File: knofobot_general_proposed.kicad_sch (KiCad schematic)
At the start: 8 parts, among them M1 Motor_DC, M2 Motor_DC, U1 L298N, U2 HC-SR04, U3 HC-SR04, U4 VL53L0CXV0DH1

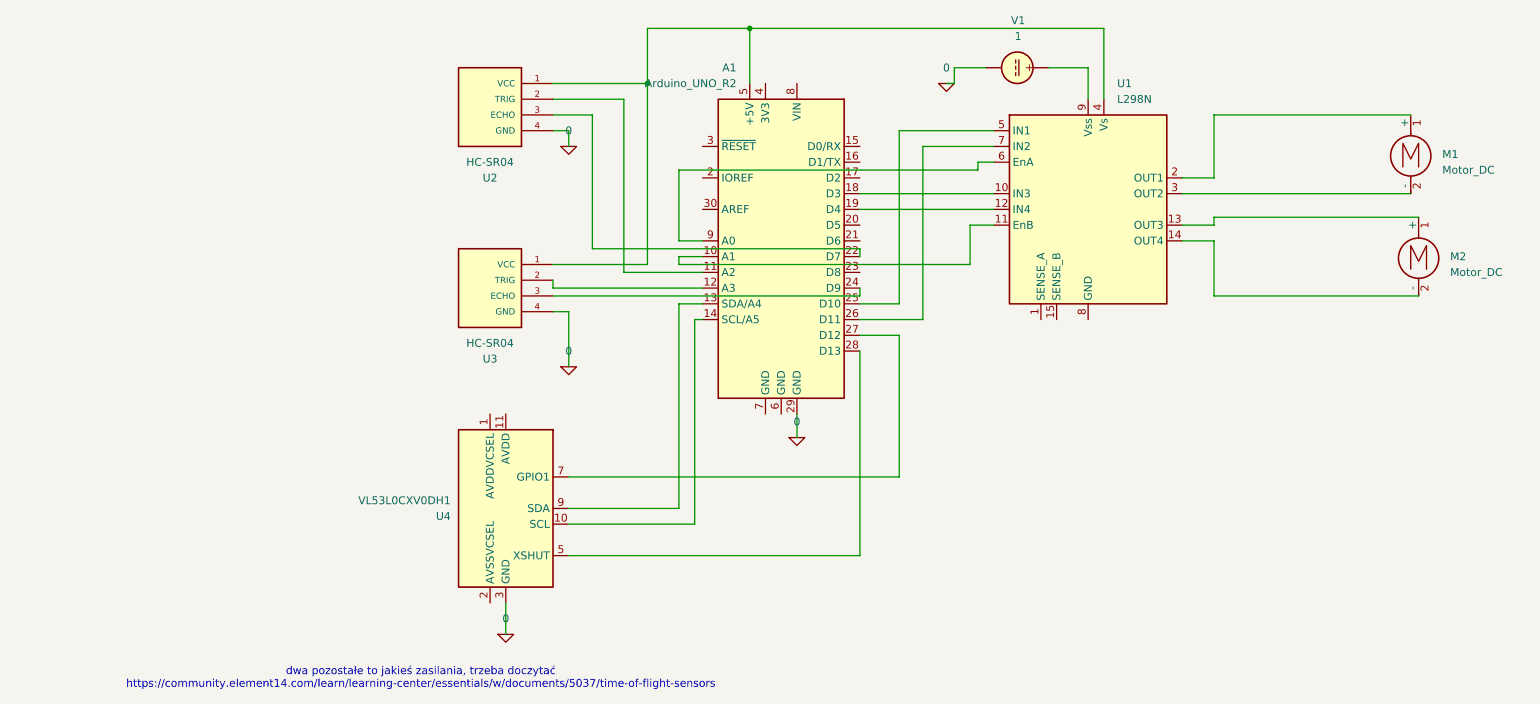
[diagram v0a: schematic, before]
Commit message: proposed new wiring minimising changes w/ 2 sensors
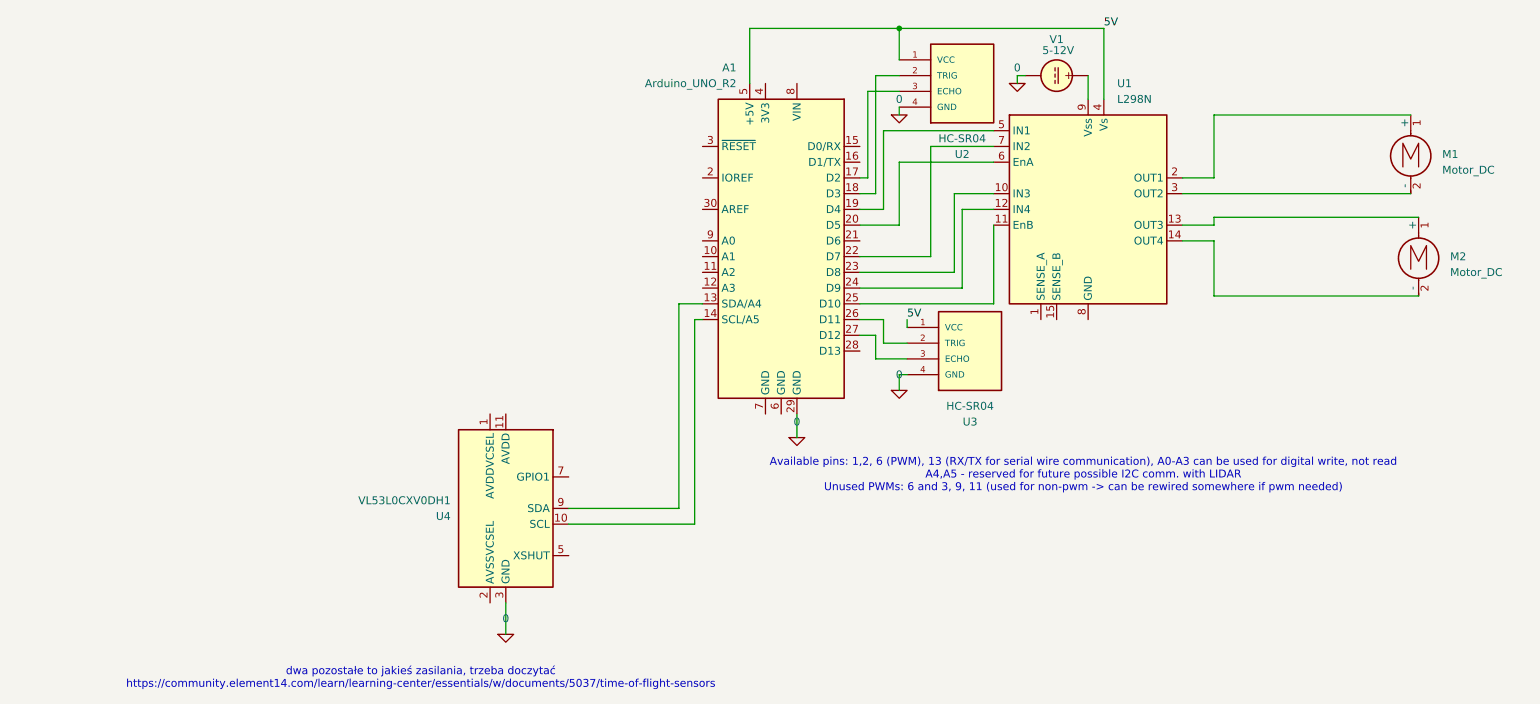
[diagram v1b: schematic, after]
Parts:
- V1: value 1 -> 5-12V
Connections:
- net at A1.10 (A1): no longer U1.11 (EnB)
- net at A1.11 (A2): no longer U2.2 (TRIG)
- net at A1.12 (A3): no longer U3.2 (TRIG)
- net at A1.17 (D2): now also U2.3 (ECHO)
- net at A1.18 (D3): now also U2.2 (TRIG); no longer U1.10 (IN3)
- net at A1.19 (D4): now also U1.5 (IN1); no longer U1.12 (IN4)
- net at A1.20 (D5): now also U1.6 (EnA)
- net at A1.22 (D7): now also U1.7 (IN2); no longer U2.3 (ECHO)
- net at A1.23 (D8): now also U1.10 (IN3)
- net at A1.24 (D9): now also U1.12 (IN4); no longer U3.3 (ECHO)
- net at A1.25 (D10): now also U1.11 (EnB); no longer U1.5 (IN1)
- net at A1.26 (D11): now also U3.2 (TRIG); no longer U1.7 (IN2)
- net at A1.27 (D12): now also U3.3 (ECHO); no longer U4.7 (GPIO1)
- net at A1.28 (D13): no longer U4.5 (XSHUT)
- net 5V: now reaches A1.5 (+5V), U1.4 (Vs), U2.1 (VCC), U3.1 (VCC)
- net at A1.9 (A0): no longer U1.6 (EnA)
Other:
- note added: "Available pins: 1,2, 6 (PWM), 13 (RX/TX for serial wire communication), A0-A3 can be used for digital write, not read A4,A5 - reserved for future possible I2C comm. with LIDAR Unused PWMs: 6 and 3, 9, 11 (used for non-pwm -> can be rewired somewhere if pwm needed)"
- moved on the sheet: U2, U3, V1
